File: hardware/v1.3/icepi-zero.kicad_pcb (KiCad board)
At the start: 4 copper layers, 65 x 30 mm, 162 parts, among them J1 Conn_02x20_Counter_Clockwise, J2 GPDI_C_1.3, J3 USB_C_Receptacle_USB2.0_14P, J4 USB_C_Receptacle_USB2.0_14P, J5 USB_C_Receptacle_USB2.0_14P, J6 Micro_SD_Card_Det2, SW1 SW_Push, SW2 SW_Push, U1 ECP5-CABGA256, U10 W9825G6KH, U11 W25Q128JVS, U2 TLV62569DBV, U3 TLV62569DBV, U4 TLV62569DBV, U5 PCA9306DC1, U6 FT231XQ, U7 TPD2EUSB30A, U8 TPD2EUSB30A, U9 TPD2EUSB30A, Y1 SG-8018CG 50.000000MHz

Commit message: Update files
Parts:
- added U12: TPD2EUSB30A, Package_TO_SOT_SMD:Texas_DRT-3, B.Cu at (129.5, 107.2)
- moved REF** 2.95 mm to (128.2, 102.0)
- moved TP5 0.16 mm to (137.0, 106.2)
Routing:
- net GND: track 99.5 -> 106.4 mm
- net /GPDI/GPDI_UTIL: track 25.5 -> 26.4 mm, vias 2 -> 3
- net /GPDI/GPDI_HPD: track 26.7 -> 27.5 mm

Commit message: Update to v1.3 board
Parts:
- added REF**: UKCA-Logo_6x6mm_SilkScreen, Symbol:UKCA-Logo_6x6mm_SilkScreen, B.Cu at (133.6, 110.4)
- moved REF** 9.10 mm to (124.8, 110.5)
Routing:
- net +5V: track 189.5 -> 196.1 mm
- net GND: track 106.4 -> 106.5 mm, vias 111 -> 109
- added copper zone on F.Cu, net +5V

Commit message: Final mass production files
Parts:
- added C37: 22uF, Capacitor_SMD:C_0603_1608Metric, B.Cu at (155.7, 116.1)
- TP1, TP2, TP3, TP4, TP5, TP6, TP7, TP8: footprint TestPoint:TestPoint_Pad_D2.0mm -> icepi-lib:TestPoint_Pad_D2.0mm_Blank
- TP10, TP11, TP12, TP13, TP14, TP9: footprint TestPoint:TestPoint_Pad_D1.0mm -> icepi-lib:TestPoint_Pad_D1.0mm_Blank
- moved TP8 0.24 mm to (144.6, 118.2)
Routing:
- net +3V3: track 93.2 -> 94.2 mm

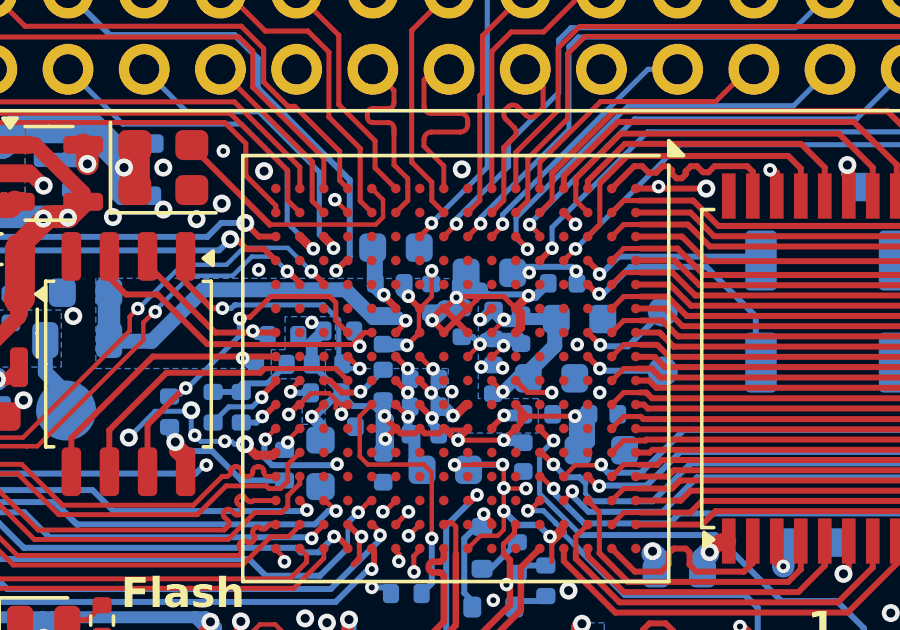
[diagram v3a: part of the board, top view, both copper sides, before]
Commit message: Improve makefile and hardware
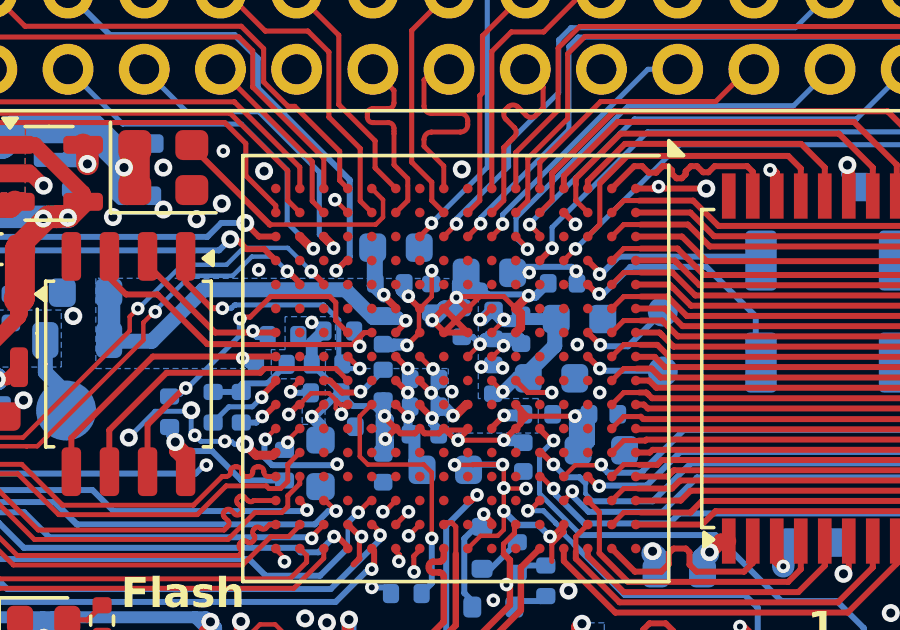
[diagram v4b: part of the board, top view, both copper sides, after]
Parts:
- renumbered C16 to C10, C4 to C11, C5 to C12, C6 to C13, C7 to C14, C20 to C15, C21 to C16, C22 to C17, C17 to C18, C18 to C19, C8 to C2, C19 to C20, C2 to C21, C45 to C22, C49 to C23, C3 to C24, C46 to C25, C50 to C26, C51 to C27, C48 to C28, C52 to C29, C9 to C3, C26 to C30, C27 to C31, C28 to C32, C23 to C33, C24 to C34, C25 to C35, C29 to C36, C30 to C37, C31 to C38, C32 to C39, C10 to C4, C33 to C40, C34 to C41, C35 to C42, C36 to C43, C38 to C44, C37 to C45, C44 to C46, C43 to C47, C41 to C48, C54 to C49, C11 to C5, C40 to C50, C39 to C51, C53 to C52, C42 to C53, C47 to C54, C12 to C6, C13 to C7, C14 to C8, C15 to C9, D13 to D10, D14 to D12, D12 to D13, D8 to D14, D4 to D2, D2 to D3, D3 to D4, D9 to D6, D6 to D7, D10 to D8, D7 to D9, J5 to J3, J3 to J5, R4 to R2, R32 to R20, R26 to R21, R34 to R22, R27 to R23, R36 to R24, R29 to R25, R37 to R26, R38 to R27, R30 to R28, R31 to R29, R2 to R3, R40 to R30, R33 to R31, R41 to R32, R35 to R33, R42 to R34, R39 to R35, R24 to R36, R25 to R37, R20 to R38, R21 to R39, R3 to R4, R22 to R40, R23 to R41, R28 to R42, R45 to R44, R44 to R45, R47 to R46, R46 to R47, TP7 to TP13, TP8 to TP14, TP13 to TP7, TP14 to TP8, U7 to U10, U10 to U11, U11 to U12, U12 to U5, U5 to U6, U9 to U7, U6 to U9
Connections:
- net /USB/D0A+ renamed /USB/D0I+
- net /USB/D0A- renamed /USB/D0I-
- net /USB/D1A+ renamed /USB/D1I+
- net /USB/D1A- renamed /USB/D1I-
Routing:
- net +3V3: track 94.2 -> 95.1 mm
